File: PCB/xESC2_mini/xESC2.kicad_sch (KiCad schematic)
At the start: 52 parts, among them J1 Conn_01x06_Male, J2 U254-051T-4BH83-F1S, J3 Conn_01x05_Male, J4 Conn_01x05_Male, J5 Conn_01x03_Male, U5 SN65HVD232

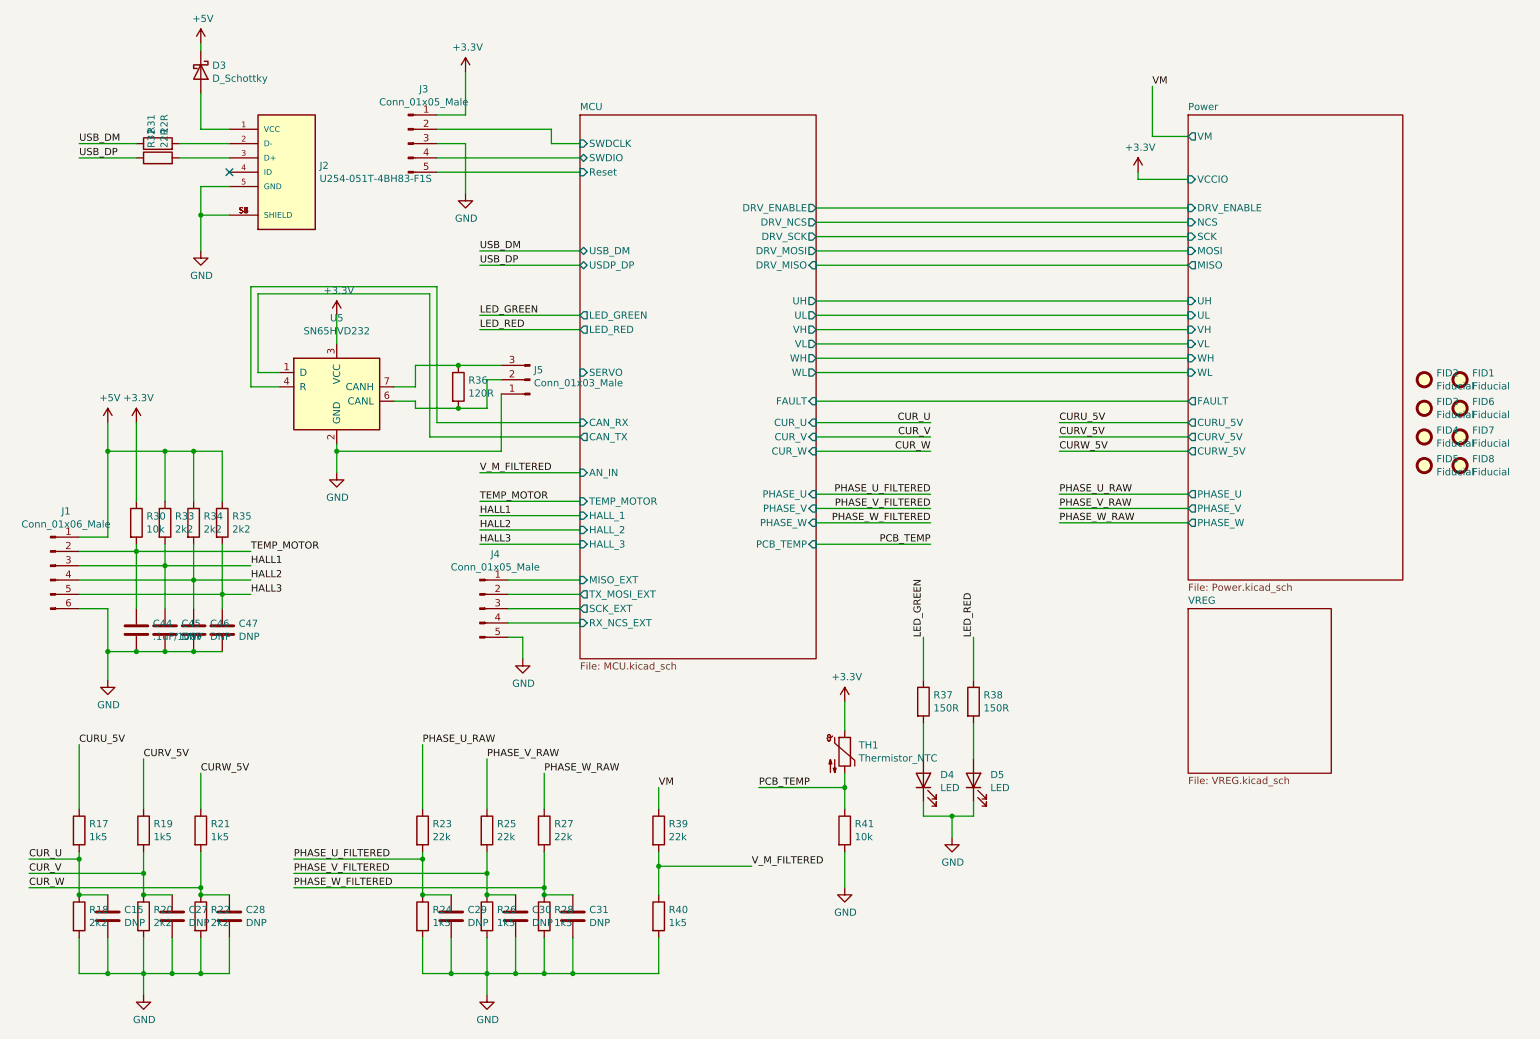
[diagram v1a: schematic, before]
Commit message: wip - most routing for RP2040 done
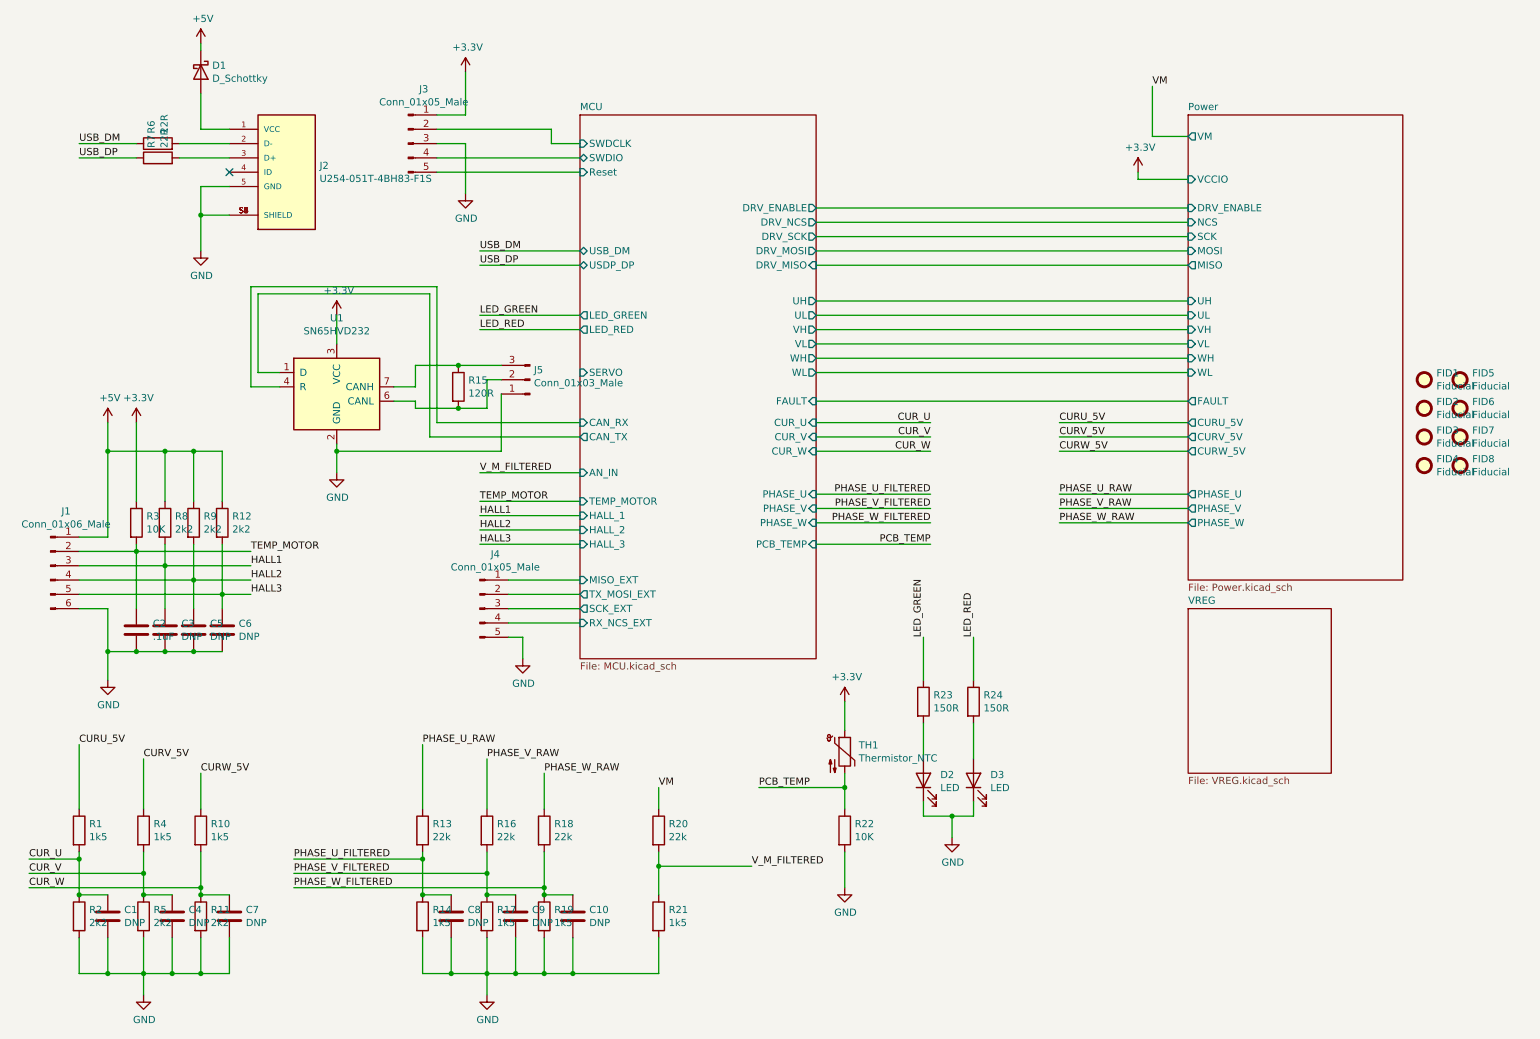
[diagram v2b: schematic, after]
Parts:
- C2: renamed from C44; value .1uF/100V -> .1uF
- R22: renamed from R41; value 10k -> 10K
- R3: renamed from R30; value 10k -> 10K
- renumbered C15 to C1, C31 to C10, C45 to C3, C27 to C4, C46 to C5, C47 to C6, C28 to C7, C29 to C8, C30 to C9, D3 to D1, D4 to D2, D5 to D3, FID2 to FID1, FID3 to FID2, FID4 to FID3, FID5 to FID4, FID1 to FID5, R17 to R1, R21 to R10, R22 to R11, R35 to R12, R23 to R13, R24 to R14, R36 to R15, R25 to R16, R26 to R17, R27 to R18, R28 to R19, R18 to R2, R39 to R20, R40 to R21, R37 to R23, R38 to R24, R19 to R4, R20 to R5, R31 to R6, R32 to R7, R33 to R8, R34 to R9, U5 to U1
